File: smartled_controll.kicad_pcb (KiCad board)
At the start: 2 copper layers, 61.2 x 43.7 mm, 96 parts, among them J1 Conn_01x04, J2 Conn_01x02, SW1 SW_Push, U1 OC5028B, U2 MAX485E, U3 PY32F003F1xUx, U4 OC5864, U5 SGM2033-3.3, U6 OC5028B, U7 GS8521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

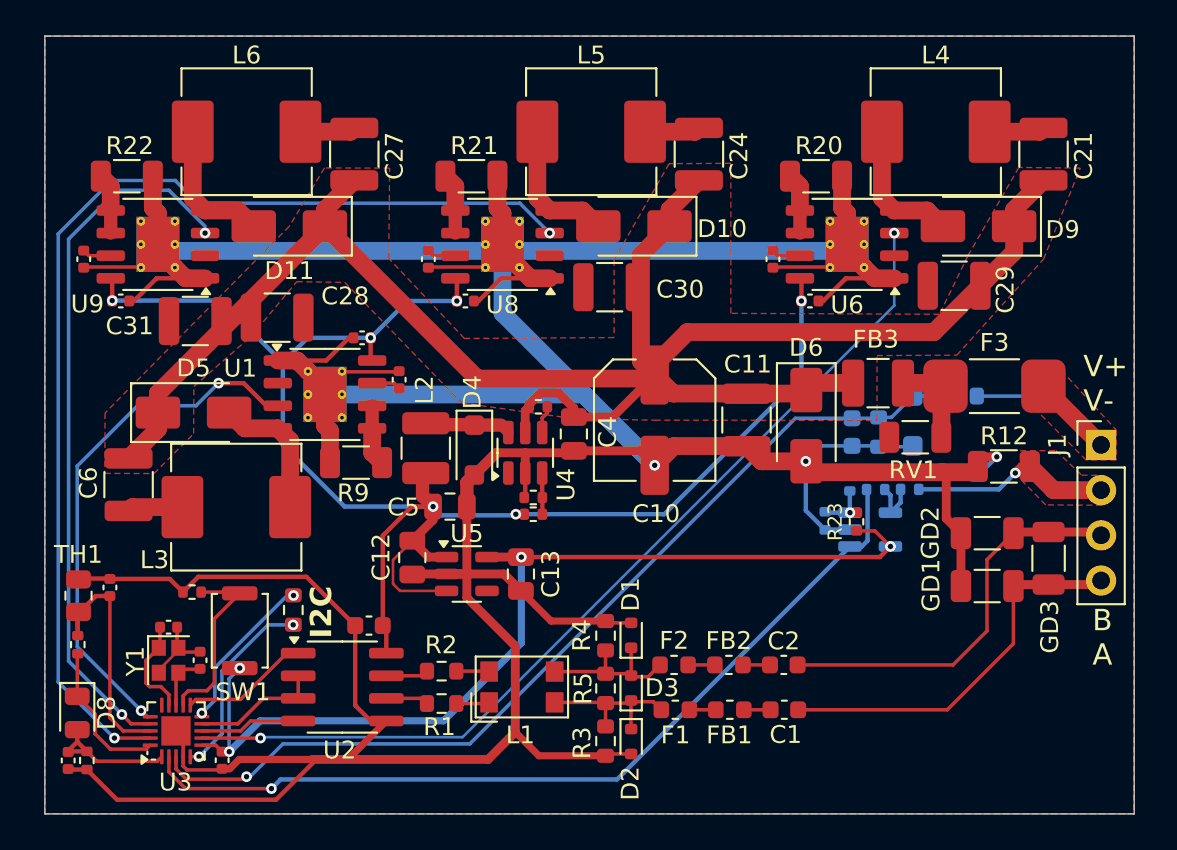
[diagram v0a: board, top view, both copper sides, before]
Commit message: 添加LED接口焊盘
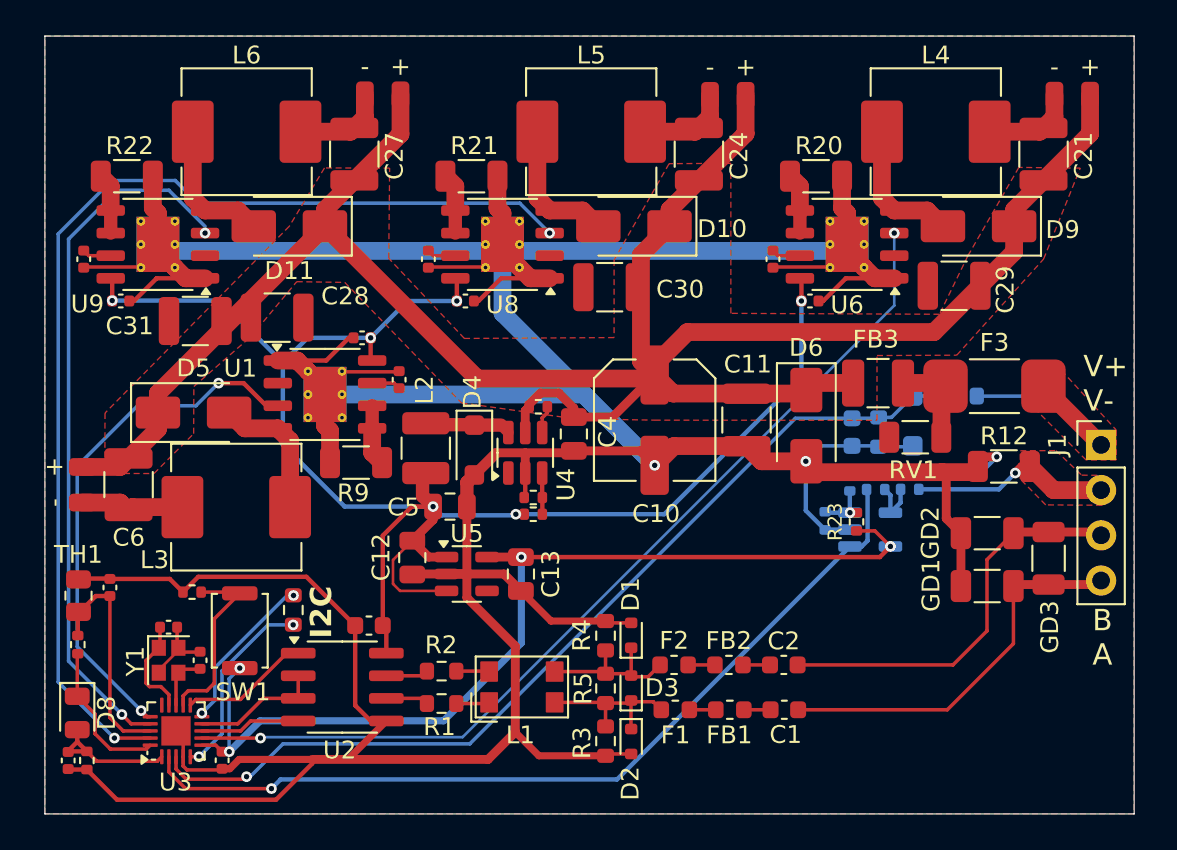
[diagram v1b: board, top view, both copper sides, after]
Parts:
- added D12: LED_Series, project_footprints:2Pads_1.0x1.5mm_P2.0mm_mpsign, F.Cu at (134.5, 77.2)
- added D13: LED_Series, project_footprints:2Pads_1.0x1.5mm_P2.0mm_mpsign, F.Cu at (190.1, 55.3)
- added D14: LED_Series, project_footprints:2Pads_1.0x1.5mm_P2.0mm_mpsign, F.Cu at (170.8, 55.3)
- added D15: LED_Series, project_footprints:2Pads_1.0x1.5mm_P2.0mm_mpsign, F.Cu at (151.4, 55.3)
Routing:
- net VINP: track 106.4 -> 126.9 mm
- net Net-(D12-K): track 3.11 -> 5.91 mm
- net Net-(D15-K): track 3.11 -> 5.22 mm
- net Net-(D13-K): track 3.11 -> 5.21 mm
- net Net-(D14-K): track 3.11 -> 5.20 mm

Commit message: 添加LED接口编号丝印
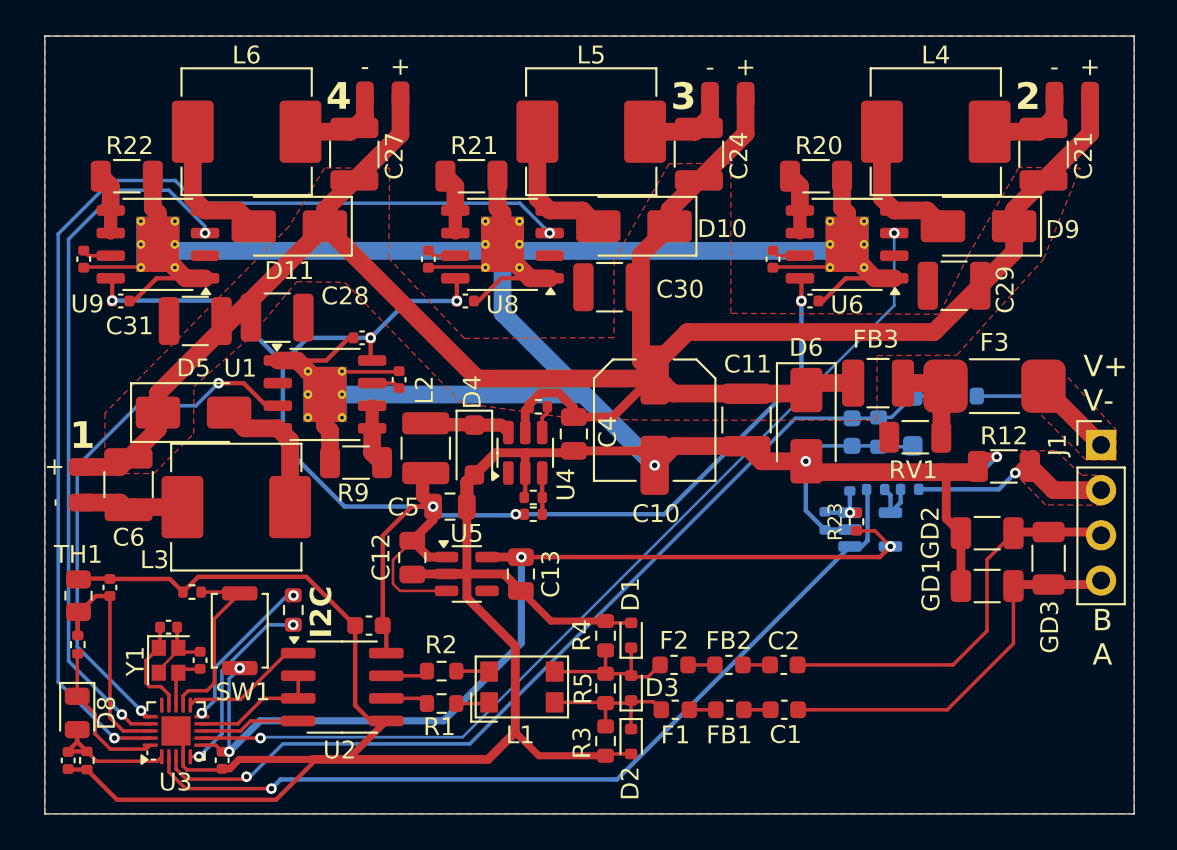
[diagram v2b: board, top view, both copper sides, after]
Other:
- board text added: "1"
- board text added: "2"
- board text added: "3"
- board text added: "4"
